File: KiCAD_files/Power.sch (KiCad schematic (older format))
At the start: 82 parts, among them J1 Screw_Terminal_01x01, J10 Conn_01x02, J13 Screw_Terminal_01x01, J14 Screw_Terminal_01x01, J15 Screw_Terminal_01x01, J17 Screw_Terminal_01x01, J2 Conn_01x06, J24 Conn_01x02, J9 Conn_01x02, Q1 QM6006D, Q2 QM6006D, Q3 Q_NIGBT_GCE, U1 ACS712xLCTR-20A, U2 MCP9700AT-ETT, U3 ACS712xLCTR-20A

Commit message: Changed project organization. Each PCB of the foreseen mezzanine has a dedicated project. Outlines and connectors between board are defined as custom footprints. Component placement is under progress for Power.pro - Measurment and Driver schematic are under progress but not frozen yet. x
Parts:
- removed J1, J13, J14, J15, J17, J? (x3): Screw_Terminal_01x01, Footprints:Connector_power, symbol Connector:Screw_Terminal_01x01
- removed J10, J24, J9: Conn_01x02, Connector_PinHeader_1.27mm:PinHeader_1x02_P1.27mm_Vertical_SMD_Pin1Right, symbol Connector_Generic:Conn_01x02
- removed J2: Conn_01x06, Connector_PinHeader_1.27mm:PinHeader_1x06_P1.27mm_Vertical_SMD_Pin1Right, symbol Connector_Generic:Conn_01x06
- removed JP2: Jumper, Footprints:HARWIN_Jumper, symbol Device:Jumper
- removed J_H1, J_H?, J_L1, J_L?: Conn_01x04, Connector_PinHeader_1.27mm:PinHeader_1x04_P1.27mm_Vertical_SMD_Pin1Right, symbol Connector_Generic:Conn_01x04
- removed U1, U?: ACS712xLCTR-20A, Package_SO:SOIC-8_3.9x4.9mm_P1.27mm, symbol Sensor_Current:ACS712xLCTR-20A
- removed U2: MCP9700AT-ETT, Package_TO_SOT_SMD:SOT-23, symbol Sensor_Temperature:MCP9700AT-ETT
- added J1, J2, J4, J5: 2604-1102, Footprints:WAGO-2604-1102, symbol Symbols:2604-1102
- added J3: Board_outline, Footprints:Board outline, symbol Symbols:Board_outline
- added R_GH3, R_GH4, R_GH5, R_GH6: 0, Resistor_SMD:R_0805_2012Metric, symbol Device:R
- added Rv1, Rv2, Rv3, Rv4, Rv5, Rv6: R_Small, Resistor_SMD:R_0805_2012Metric, symbol Device:R_Small
- added U1, U4: ACS730xLCTR-20AB, Package_SO:SOIC-8_3.9x4.9mm_P1.27mm, symbol Sensor_Current:ACS730xLCTR-20AB
- added U2: LM35-LP, Package_TO_SOT_THT:TO-92, symbol Sensor_Temperature:LM35-LP
- F1, F2, F3, F4: renamed from F?; footprint (none) -> Footprints:RKEF500
- L1: footprint Footprints:Inductor_WE-HCF_2818 -> Footprints:WE-HCF-2013
- L2: renamed from L?; footprint Footprints:Inductor_WE-HCF_2818 -> Footprints:WE-HCF-2013
- Q3: footprint Footprints:TO-252-2-modified -> Package_TO_SOT_SMD:TO-252-2
- gave numbers to parts that had none: 30
- renumbered C25 to C13, C23 to C15, C26 to C17, C27 to C3, C28 to C7, C3 to C9
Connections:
- net labels added: +5VD, DGND, IIHigh, IILow1, IILow2, Neutral_GND_cmd, PWM_H1, PWM_H2, PWM_L1, PWM_L2, SW_Node1, SW_Node2, VIHigh+, VIHigh-, VILow1+, VILow1-, VILow2+, VILow2-, VTh, V_In1, V_In2
- net labels removed: +5P, Iin_raw, Iout_raw, N_GND, PWM_Hi, PWM_Lo, V_In, V_Th
- wire segments 255 -> 282
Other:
- moved on the sheet: C1, C12, C22, C3, C4, C5, C7, C9, C_1snub2, C_2snub2, D2, D3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

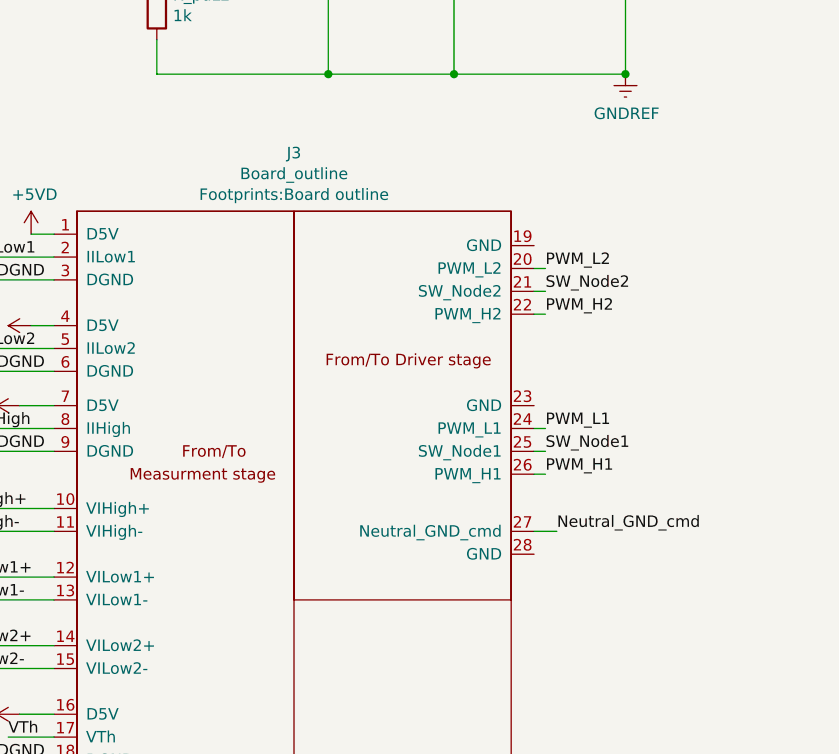
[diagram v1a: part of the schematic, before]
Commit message: Major modifications of the measurment board schematic Component placement finalized - 3D footprints added - mezzanine assembly on freecad added
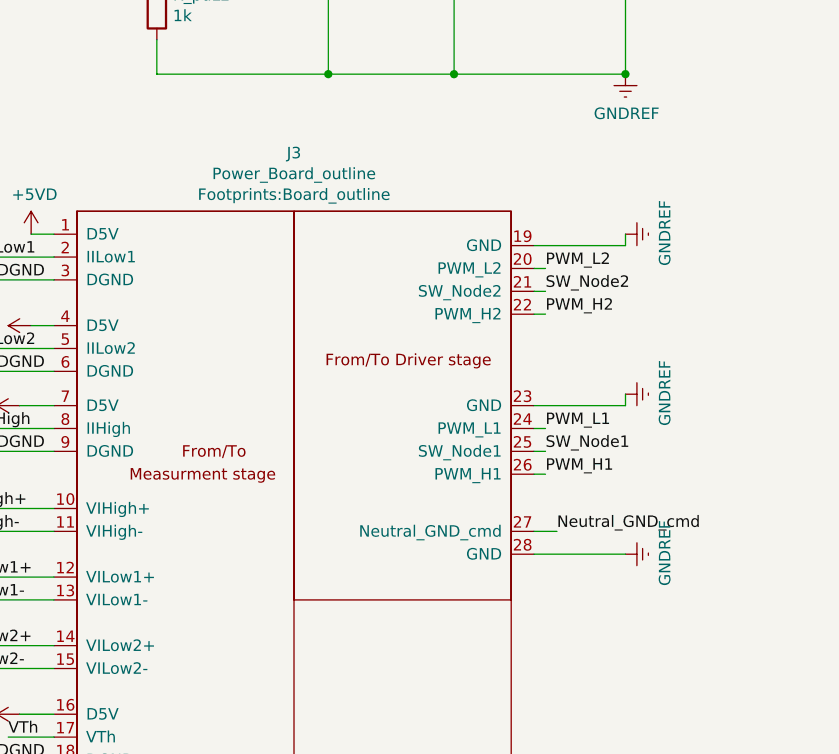
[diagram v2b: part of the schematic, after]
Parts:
- removed J3: Board_outline, Footprints:Board outline, symbol Symbols:Board_outline
- added J3: Power_Board_outline, Footprints:Board_outline, symbol Symbols:Power_Board_outline
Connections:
- net +5VD: now also J3.1 (D5V), J3.16 (D5V), J3.4 (D5V), J3.7 (D5V)
- net DGND: now also J3.18 (DGND), J3.3 (DGND), J3.6 (DGND), J3.9 (DGND)
- net GNDREF: now also J3.11 (VIHigh-), J3.19 (GND), J3.23 (GND), J3.28 (GND)
- net IIHigh: now also J3.8 (IIHigh)
- net IILow1: now also J3.2 (IILow1)
- net IILow2: now also J3.5 (IILow2)
- net N: now also J3.13 (VILow1-), J3.15 (VILow2-)
- net Neutral_GND_cmd: now also J3.27 (Neutral_GND_cmd)
- net PWM_H1: now also J3.26 (PWM_H1)
- net PWM_H2: now also J3.22 (PWM_H2)
- net PWM_L1: now also J3.24 (PWM_L1)
- net PWM_L2: now also J3.20 (PWM_L2)
- net SW_Node1: now also J3.25 (SW_Node1)
- net SW_Node2: now also J3.21 (SW_Node2)
- net VIHigh+: now also J3.10 (VIHigh+)
- net VILow1+: now also J3.12 (VILow1+)
- net VILow2+: now also J3.14 (VILow2+)
- net VTh: now also J3.17 (VTh)
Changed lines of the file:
@@
-	1    0    0    -1
-$EndComp
-$Comp
-L Symbols:Board_outline J3
-U 1 1 5F345E50
-P 8200 9400
-F 0 "J3" H 8250 10805 50  0000 C CNN
-F 1 "Board_outline" H 8250 10714 50  0000 C CNN
-F 2 "Footprints:Board outline" H 8250 10623 50  0000 C CNN
-F 3 "" H 8450 8450 50  0001 C CNN
-	1    8200 9400
 	1    0    0    -1
 $EndComp
@@
 $EndComp
 $Comp
-L power:+5VD #PWR?
+L power:+5VD #PWR0104
 U 1 1 5F3591CB
 P 7100 8350
-F 0 "#PWR?" H 7100 8200 50  0001 C CNN
+F 0 "#PWR0104" H 7100 8200 50  0001 C CNN
 F 1 "+5VD" H 7115 8523 50  0000 C CNN
 F 2 "" H 7100 8350 50  0001 C CNN
@@
 	7100 8750 7200 8750
 $Comp
-L power:+5VD #PWR?
+L power:+5VD #PWR0105
 U 1 1 5F39D657
 P 7100 8750
-F 0 "#PWR?" H 7100 8600 50  0001 C CNN
+F 0 "#PWR0105" H 7100 8600 50  0001 C CNN
 F 1 "+5VD" H 7115 8923 50  0000 C CNN
 F 2 "" H 7100 8750 50  0001 C CNN
@@
 $EndComp
 $Comp
-L power:+5VD #PWR?
+L power:+5VD #PWR0108
 U 1 1 5F3C969E
 P 7050 9100
-F 0 "#PWR?" H 7050 8950 50  0001 C CNN
+F 0 "#PWR0108" H 7050 8950 50  0001 C CNN
 F 1 "+5VD" H 7065 9273 50  0000 C CNN
 F 2 "" H 7050 9100 50  0001 C CNN
@@
 	7200 9100 7050 9100
 $Comp
-L power:+5VD #PWR?
+L power:+5VD #PWR0109
 U 1 1 5F40B048
 P 7050 10450
-F 0 "#PWR?" H 7050 10300 50  0001 C CNN
+F 0 "#PWR0109" H 7050 10300 50  0001 C CNN
 F 1 "+5VD" H 7065 10623 50  0000 C CNN
 F 2 "" H 7050 10450 50  0001 C CNN
@@
 Wire Wire Line
 	7200 10450 7050 10450
+$Comp
+L power:GNDREF #PWR?
+U 1 1 60571F0C
+P 9700 8350
+AR Path="/5E91AAF4/60571F0C" Ref="#PWR?"  Part="1"
+AR Path="/5E86B783/60571F0C" Ref="#PWR?"  Part="1"
+AR Path="/5E99427A/60571F0C" Ref="#PWR?"  Part="1"
+AR Path="/60571F0C" Ref="#PWR0111"  Part="1"
+F 0 "#PWR0111" H 9700 8100 50  0001 C CNN
+F 1 "GNDREF" H 9705 8177 50  0000 C CNN
+F 2 "" H 9700 8350 50  0001 C CNN
+F 3 "" H 9700 8350 50  0001 C CNN
+	1    9700 8350
+	0    -1   -1   0
+$EndComp
+$Comp
+L power:GNDREF #PWR?
+U 1 1 605886E1
+P 9700 9050
+AR Path="/5E91AAF4/605886E1" Ref="#PWR?"  Part="1"
+AR Path="/5E86B783/605886E1" Ref="#PWR?"  Part="1"
+AR Path="/5E99427A/605886E1" Ref="#PWR?"  Part="1"
+AR Path="/605886E1" Ref="#PWR0112"  Part="1"
+F 0 "#PWR0112" H 9700 8800 50  0001 C CNN
+F 1 "GNDREF" H 9705 8877 50  0000 C CNN
+F 2 "" H 9700 9050 50  0001 C CNN
+F 3 "" H 9700 9050 50  0001 C CNN
+	1    9700 9050
+	0    -1   -1   0
+$EndComp
+$Comp
+L power:GNDREF #PWR?
+U 1 1 6059EAC3
+P 9700 9750
+AR Path="/5E91AAF4/6059EAC3" Ref="#PWR?"  Part="1"
+AR Path="/5E86B783/6059EAC3" Ref="#PWR?"  Part="1"
+AR Path="/5E99427A/6059EAC3" Ref="#PWR?"  Part="1"
+AR Path="/6059EAC3" Ref="#PWR0113"  Part="1"
+F 0 "#PWR0113" H 9700 9500 50  0001 C CNN
+F 1 "GNDREF" H 9705 9577 50  0000 C CNN
+F 2 "" H 9700 9750 50  0001 C CNN
+F 3 "" H 9700 9750 50  0001 C CNN
+	1    9700 9750
+	0    -1   -1   0
+$EndComp
+Wire Wire Line
+	9300 9750 9700 9750
+Wire Wire Line
+	9300 9100 9700 9100
+Wire Wire Line
+	9700 9100 9700 9050
+Wire Wire Line
+	9300 8400 9700 8400
+Wire Wire Line
+	9700 8400 9700 8350
+$Comp
+L Symbols:Power_Board_outline J3
+U 1 1 5F4B4102
+P 8200 9400
+F 0 "J3" H 8250 10805 50  0000 C CNN
+F 1 "Power_Board_outline" H 8250 10714 50  0000 C CNN
+F 2 "Footprints:Board_outline" H 8250 10623 50  0000 C CNN
+F 3 "" H 8450 8450 50  0001 C CNN
+	1    8200 9400
+	1    0    0    -1
+$EndComp
 $EndSCHEMATC
